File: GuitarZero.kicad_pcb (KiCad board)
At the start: 6 copper layers, 144 parts, among them J1 USB_A, J2 USB_B_Micro, J3 AudioJack3_SwitchT, J4 MCU_Debug, J6 Micro_SD_Card_Det_Hirose_DM3AT, SW1 SW_Push, SW2 SW_Push, SW3 SW_Push, SW4 SW_Push, SW5 SW_Push, SW6 SW_Push, U1 TPS54325, U10 FPGA_GPIO_Extra, U11 5x7 LED_matrix, U12 MCU_GPIO_Extra, U13 5x7 LED_matrix, U14 Power_Jumpers, U2 TSP54294, U3 XC7A100T-FTG256, U4 EFM32GG332, U5 S25FL127S, U6 Oscillator, U7 FPGA_JTAG_Debug, U8 PCM1754, U9 TPD_Current_Switch, Y1 Crystal_GND23

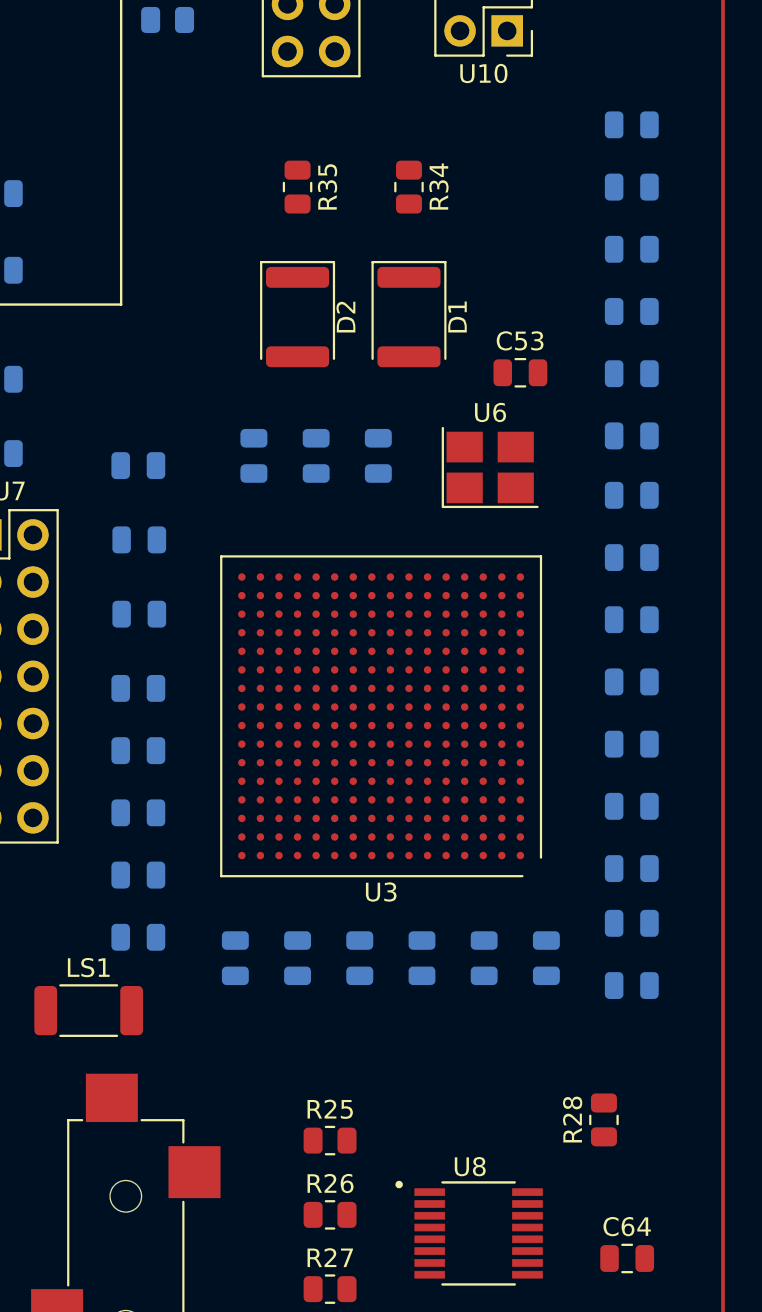
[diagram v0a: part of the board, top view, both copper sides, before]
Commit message: Resized Capacitors
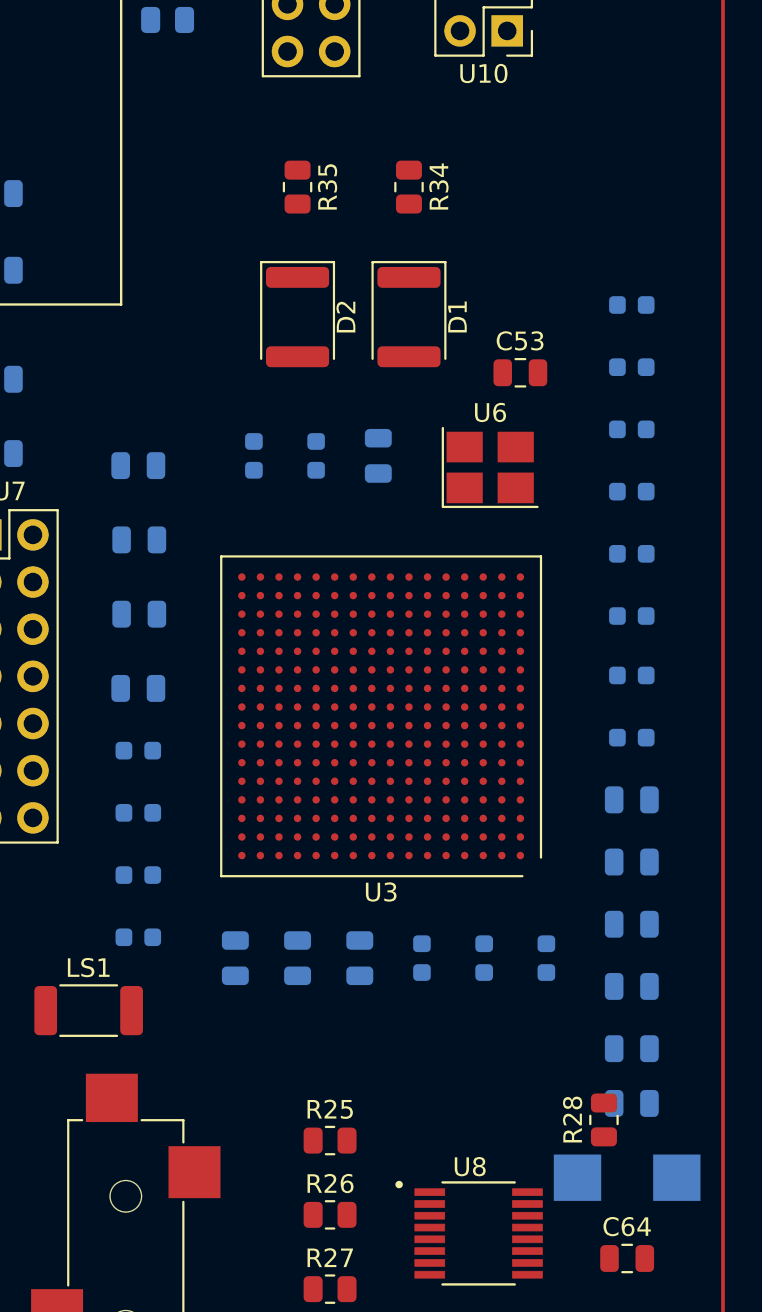
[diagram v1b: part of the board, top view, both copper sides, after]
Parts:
- C20: footprint Capacitor_SMD:C_0805_2012Metric -> T520V337M2R5ATE025:CAPMP7.6X4.3_1.9N_KEM
- C27, C28, C29, C30, C31, C32, C33, C34, C36, C37, C41, C42, C43, C48, C49, C50, C51: footprint Capacitor_SMD:C_0805_2012Metric -> Capacitor_SMD:C_0603_1608Metric
- moved C20 10.4 mm to (211.0, 128.0)
- moved C21 9.70 mm to (211.2, 124.0)
- moved C22 9.70 mm to (211.2, 121.0)
- moved C23 9.70 mm to (211.2, 117.7)
- moved C25 9.70 mm to (211.2, 111.0)
- moved C26 9.70 mm to (211.2, 107.7)
- moved C27 9.70 mm to (211.2, 104.3)
- moved C28 9.70 mm to (211.2, 101.0)
- moved C29 9.70 mm to (211.2, 97.8)
- moved C30 9.70 mm to (211.2, 94.4)
- moved C31 9.70 mm to (211.2, 91.0)
- moved C32 9.70 mm to (211.2, 87.7)
- moved C34 9.70 mm to (211.2, 81.0)
- moved C24 9.70 mm to (211.2, 114.3)
- moved C33 9.70 mm to (211.2, 84.3)
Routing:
- added copper zone on In3.Cu, net +3.3V
- added copper zone on In1.Cu, net GND
- removed copper zone on In2.Cu, net GND

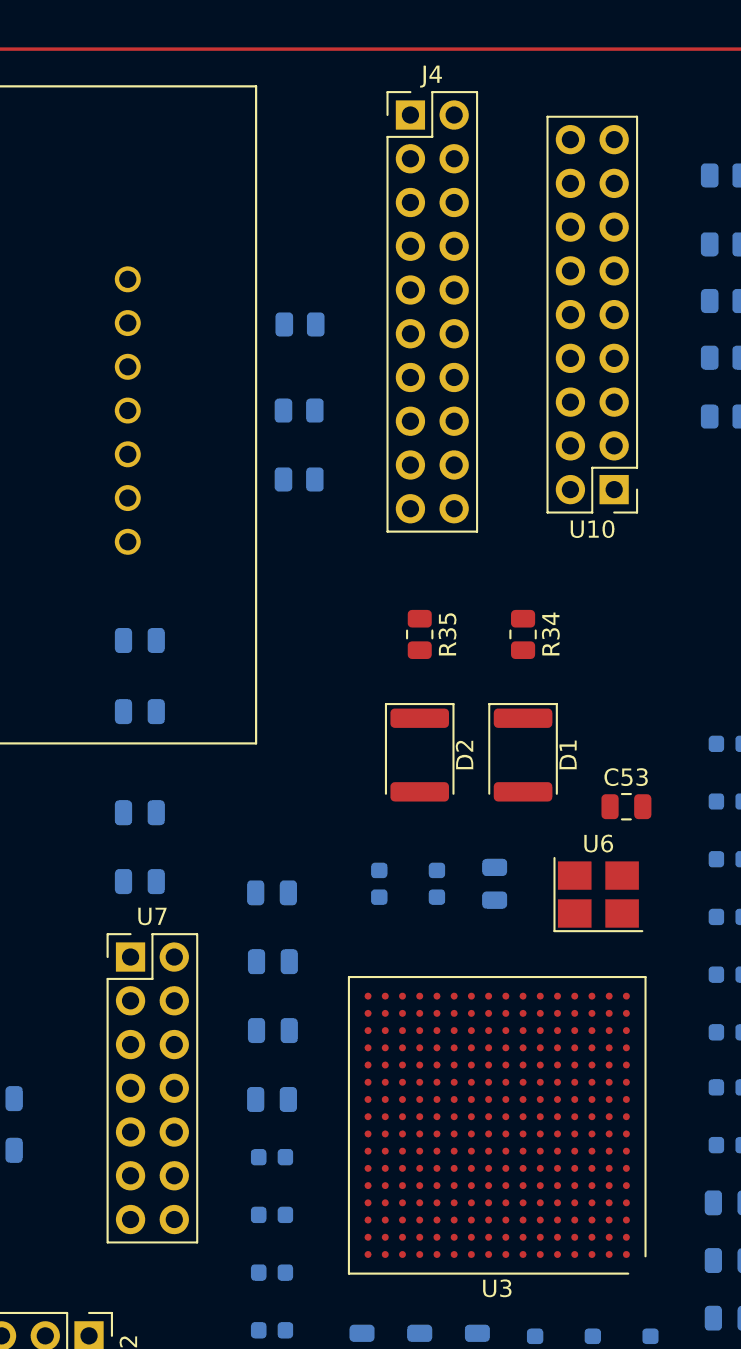
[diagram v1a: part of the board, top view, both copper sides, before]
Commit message: Changed FPGA_Debug to 2mm pitch and updated PCB
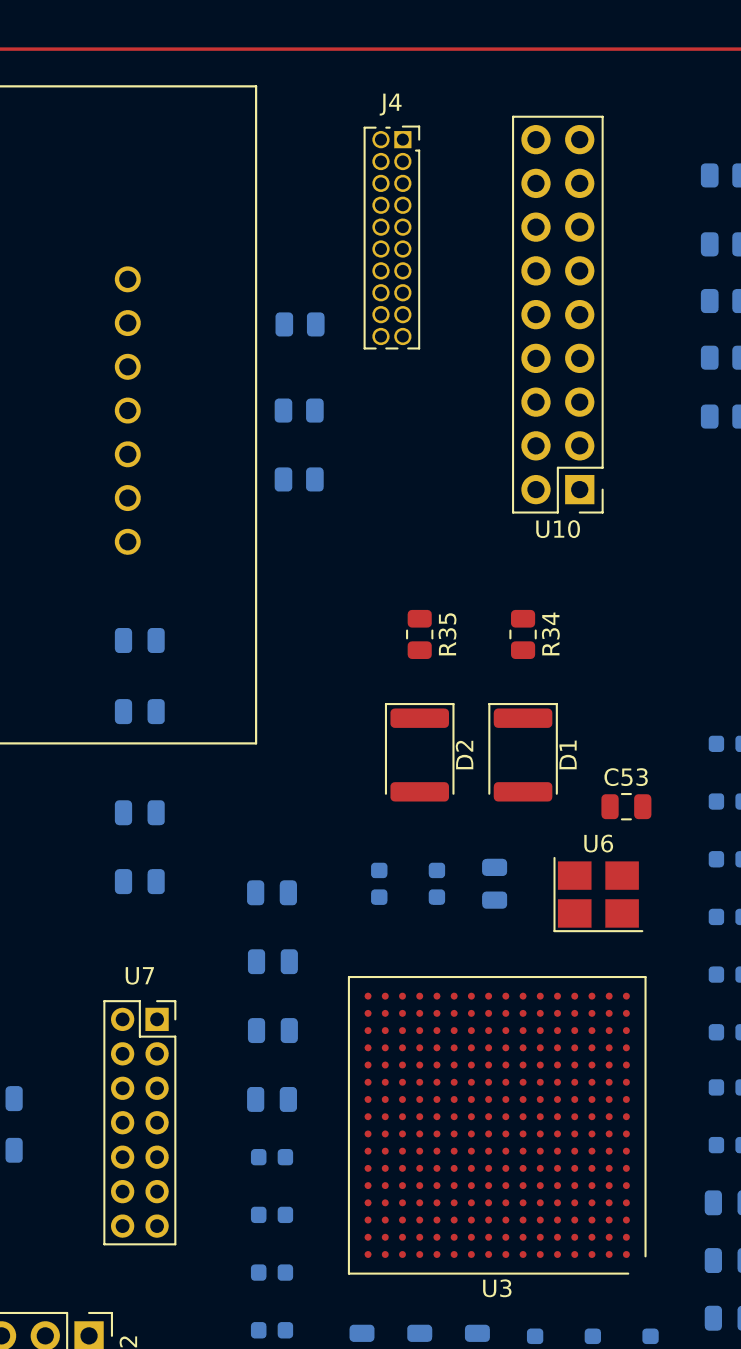
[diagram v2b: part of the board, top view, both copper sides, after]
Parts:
- J4: footprint Connector_PinHeader_2.54mm:PinHeader_2x10_P2.54mm_Vertical -> Connector_PinSocket_1.27mm:PinSocket_2x10_P1.27mm_Vertical
- U7: footprint Connector_PinHeader_2.54mm:PinHeader_2x07_P2.54mm_Vertical -> Connector_PinSocket_2.00mm:PinSocket_2x07_P2.00mm_Vertical
- moved U7 3.93 mm to (178.0, 97.0)
- moved U10 2.00 mm to (202.5, 66.2)
- moved J4 1.50 mm to (192.3, 45.9)

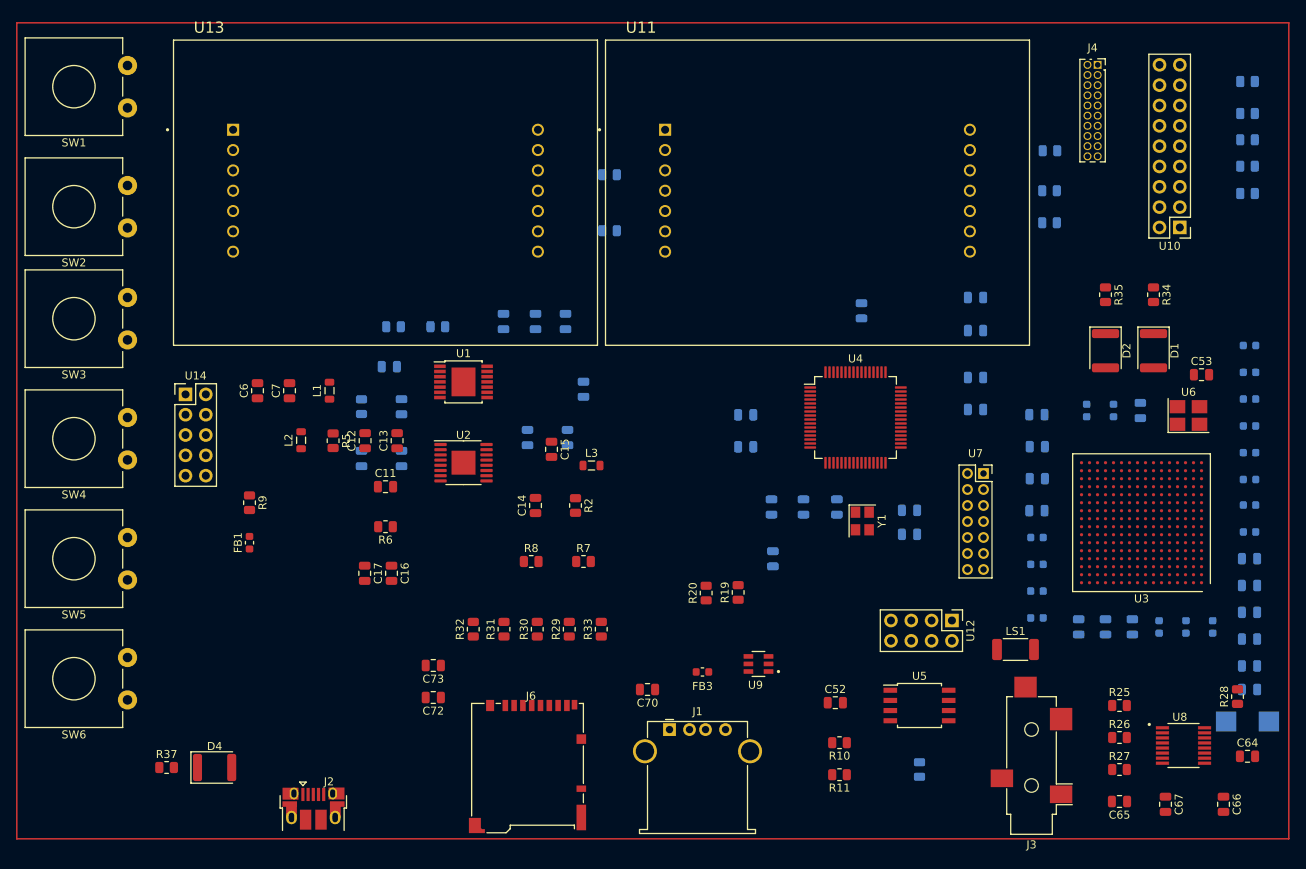
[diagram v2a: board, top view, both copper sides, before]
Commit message: Made room for PSU heatsinks
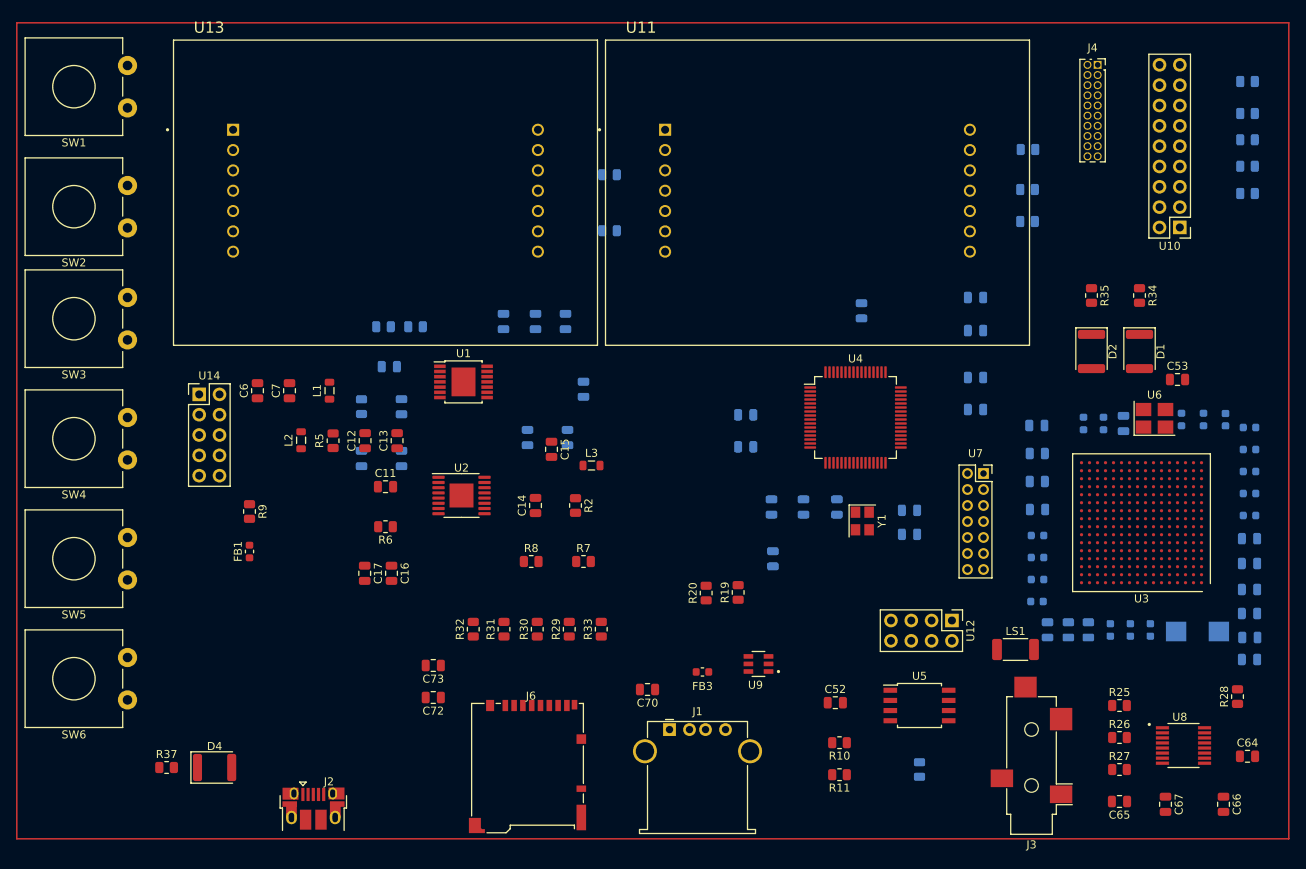
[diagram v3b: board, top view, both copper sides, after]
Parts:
- moved C20 12.9 mm to (204.8, 116.8), turned to 180 degrees
- moved C34 12.6 mm to (202.8, 90.2), turned to 90 degrees
- moved C33 8.24 mm to (205.5, 90.2), turned to 90 degrees
- moved C43 7.81 mm to (198.8, 116.5)
- moved C42 6.96 mm to (196.3, 116.5)
- moved C41 6.11 mm to (193.8, 116.5)
- moved C40 5.51 mm to (191.1, 116.5)
- moved C39 4.67 mm to (188.6, 116.5)
- moved U6 4.26 mm to (199.4, 90.1)
- moved U2 4.11 mm to (112.8, 99.8)
- moved C32 3.95 mm to (208.2, 90.3), turned to 90 degrees
- moved C38 3.92 mm to (186.0, 116.5)
- moved C21 3.75 mm to (211.2, 120.2)
- moved C22 3.55 mm to (211.3, 117.5)
- moved C23 3.20 mm to (211.2, 114.5)
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
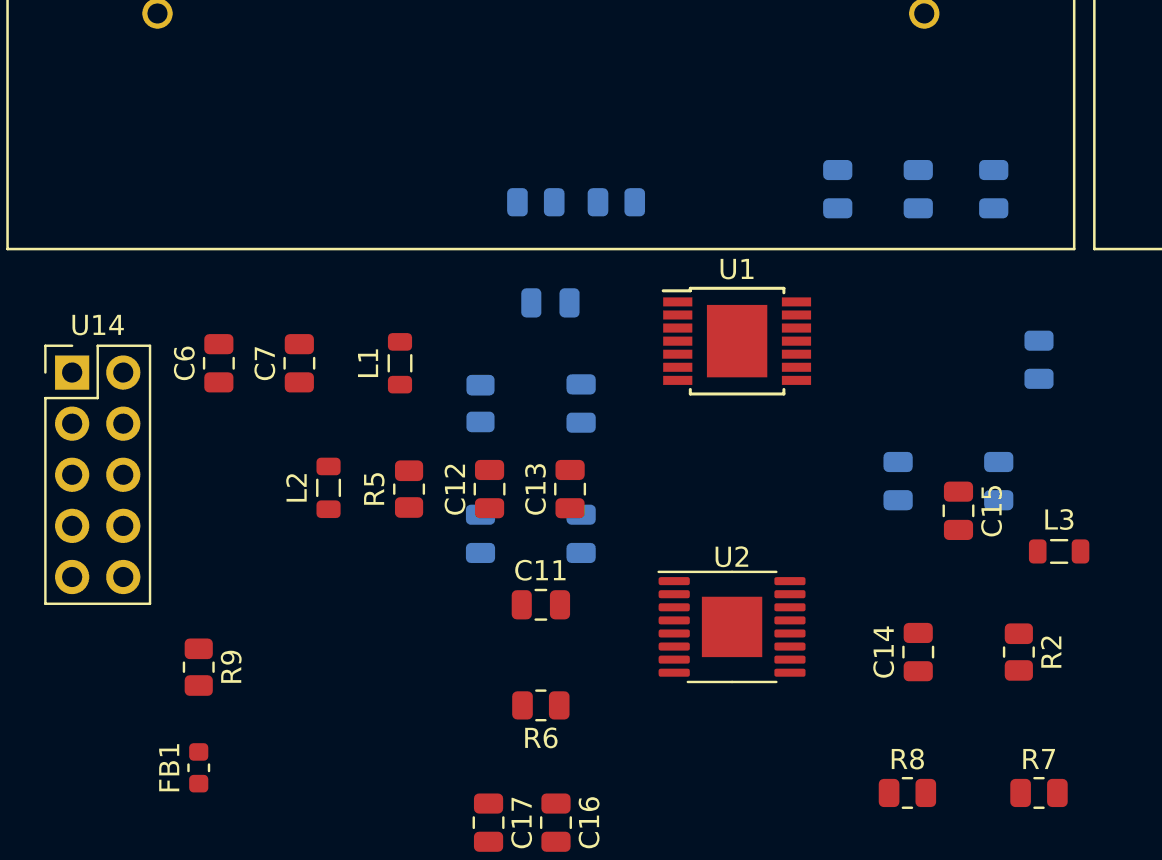
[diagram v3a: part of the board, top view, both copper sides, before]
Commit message: start of psu routing
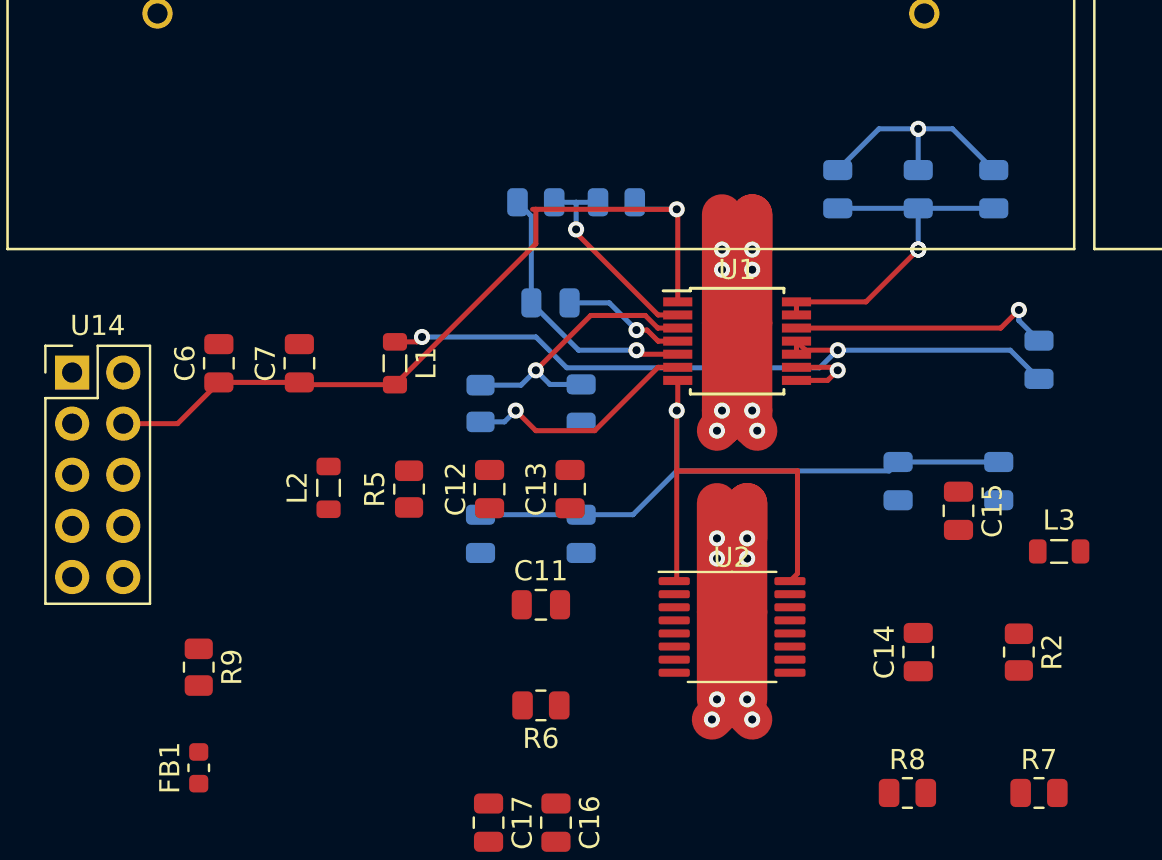
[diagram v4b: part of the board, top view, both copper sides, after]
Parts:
- moved L1 0.25 mm to (96.0, 86.7), turned to -90 degrees
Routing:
- net +5V: track 0.00 -> 84.4 mm, vias 0 -> 3
- net GND: track 0.00 -> 77.0 mm, vias 0 -> 19
- net /PSU/+1V0: track 0.00 -> 40.0 mm, vias 0 -> 1
- net Net-(U1-SW1): track 0.00 -> 36.6 mm, vias 0 -> 2
- net Net-(U1-VREG5): track 0.00 -> 14.0 mm, vias 0 -> 1
- net Net-(U1-VBST): track 0.00 -> 13.4 mm, vias 0 -> 1
- net Net-(U1-PG): track 0.00 -> 11.8 mm, vias 0 -> 1
- net Net-(U1-VFB): track 0.00 -> 10.4 mm, vias 0 -> 1
- net Net-(U1-SS): track 0.00 -> 6.16 mm, vias 0 -> 1

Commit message: Finish Routing of PSU
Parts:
- C16, C17, FB1, R7, R8, R9: moved to B.Cu
- moved C17 27.0 mm to (127.7, 109.6), turned to 180 degrees
- moved C16 19.6 mm to (123.6, 109.6), turned to 180 degrees
- moved C15 4.22 mm to (121.0, 97.0)
- moved R7 3.62 mm to (129.0, 104.5)
- moved R8 3.62 mm to (122.5, 104.5)
- moved FB1 3.23 mm to (85.7, 103.6)
- moved R9 2.25 mm to (85.7, 99.6)
- moved R5 1.26 mm to (96.0, 94.0), turned to 90 degrees
- moved L2 1.15 mm to (93.0, 94.0), turned to -90 degrees
- moved C12 1.00 mm to (101.0, 92.0)
- moved C13 1.00 mm to (105.0, 92.0)
- turned C11 to 180 degrees
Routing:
- net +5V: track 84.4 -> 201.0 mm, vias 3 -> 4
- net /PSU/+3.3V: track 0.00 -> 86.1 mm, vias 0 -> 1
- net GND: track 77.0 -> 143.0 mm, vias 19 -> 25
- net /PSU/+1V8: track 0.00 -> 27.7 mm
- net Net-(U2-EN2): track 0.00 -> 24.2 mm, vias 0 -> 2
- net Net-(U2-SW1): track 0.00 -> 23.0 mm, vias 0 -> 2
- net Net-(U2-VFB1): track 0.00 -> 22.6 mm
- net Net-(U2-SW2): track 0.00 -> 13.5 mm
- net Net-(U2-VREG5): track 0.00 -> 11.4 mm
- net Net-(U2-VBST2): track 0.00 -> 6.26 mm
- net Net-(U2-VBST1): track 0.00 -> 5.89 mm
- net Net-(U2-VFB2): track 0.00 -> 4.71 mm
- net /PSU/+3.3VA: track 0.00 -> 3.76 mm
- net Net-(D4-K): track 0.00 -> 2.95 mm
- net Net-(FB1-Pad2): track 0.00 -> 2.30 mm
